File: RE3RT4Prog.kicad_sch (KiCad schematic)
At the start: 47 parts, among them J1 Conn_01x08, J2 Conn_01x08, Q1 BD140, Q2 2N7000, Q3 2N7000, Q4 2N7000, U1 DG408, U2 155RE3, U3 556RT4, U4 74HC164

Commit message: Schema almost done
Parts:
- added C1, C2: 22, symbol Device:C
- added C3: 0.1, symbol Device:C
- added C4, C5, C7, C8, C9: 1.0, symbol Device:C
- added C6: 10.0, symbol Device:C
- added J3: DE9_Receptacle_MountingHoles, Connector_Dsub:DSUB-9_Female_Horizontal_P2.77x2.84mm_EdgePinOffset4.94mm_Housed_MountingHolesOffset7.48mm, symbol Connector:DE9_Receptacle_MountingHoles
- added J4, J5: Conn_01x02, Connector_PinHeader_2.54mm:PinHeader_1x02_P2.54mm_Vertical, symbol Connector_Generic:Conn_01x02
- added J6: PicKit, Connector_PinHeader_2.54mm:PinHeader_1x05_P2.54mm_Vertical, symbol Connector_Generic:Conn_01x05
- added J7: Barrel_Jack_MountingPin, Connector_BarrelJack:BarrelJack_GCT_DCJ200-10-A_Horizontal, symbol Connector:Barrel_Jack_MountingPin
- added TP12: +5V, symbol Connector:TestPoint
- added TP13: GND, symbol Connector:TestPoint
- added TP14: +12V, symbol Connector:TestPoint
- added U6: PIC18F26K22-xSP, Package_DIP:DIP-28_W7.62mm_Socket_LongPads, symbol MCU_Microchip_PIC18:PIC18F26K22-xSP
- added U7: MAX232, Package_DIP:DIP-16_W7.62mm_Socket_LongPads, symbol Interface_UART:MAX232
- added Y1: 7.3728, Crystal:Crystal_HC49-U_Vertical, symbol Device:Crystal
- R15: value R -> 2k
- R16: value R -> 100k
- R17, R18: value R -> 100
- R19, R20: value R -> 22
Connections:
- net +12V: now also TP14.1
- net +5V: now also C7.1, J4.1 (Pin_1), J4.2 (Pin_2), J6.2 (Pin_2), J7.1, TP12.1, U7.16 (VCC)
- net B0: now also U6.21 (RB0)
- net B1: now also U6.22 (RB1)
- net B2: now also U6.23 (RB2)
- net CE: now also U6.13 (RC2)
- net CLK: now also U6.14 (RC3)
- net CLR: now also U6.15 (RC4)
- net GND: now also R17.2, R18.2, C1.2, C2.2, C3.2, C6.2, C7.2, C8.2, C9.2, J3.0 (PAD), J3.5, J5.1 (Pin_1), J5.2 (Pin_2), J6.3 (Pin_3), J7.2, TP13.1, U6.19 (VSS), U6.8 (VSS), U7.15 (GND)
- net RD: now also U6.25 (RB4)
- net SER: now also U6.16 (RC5)
- net WR: now also U6.24 (RB3)
- net at R17.1: now also U7.10 (T2IN)
- net at R19.1: now also U7.14 (T1OUT)
- net at R19.2: now also J3.2
- net at R18.1: now also U7.8 (R2IN)
- net at R16.1: now also C3.1, U6.20 (VDD)
- net at R16.2: now also R15.2, C6.1
- net MCLR: now reaches R15.1
- net MCLR: now also J6.1 (Pin_1), U6.1 (~{MCLR}/VPP/RE3)
- net at R20.1: now also U7.13 (R1IN)
- net at R20.2: now also J3.3
- new net: C2.1, U6.10 (RA6/OSC2_CLKOUT), Y1.1
- new net: C1.1, U6.9 (RA7/OSC1_CLKIN), Y1.2
- new net: C8.1, U7.2 (VS+)
- new net: C5.1, U7.4 (C2+)
- new net: C5.2, U7.5 (C2-)
- new net: C4.1, U7.1 (C1+)
- new net: C4.2, U7.3 (C1-)
- new net: C9.1, U7.6 (VS-)
- new net PGC: J6.5 (Pin_5), U6.27 (RB6/PGC)
- new net PGD: J6.4 (Pin_4), U6.28 (RB7/PGD)
- new net RX: U6.18 (RC7), U7.12 (R1OUT)
- new net TX: U6.17 (RC6), U7.11 (T1IN)
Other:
- moved on the sheet: R15, R16, R17, R18, R19, R20

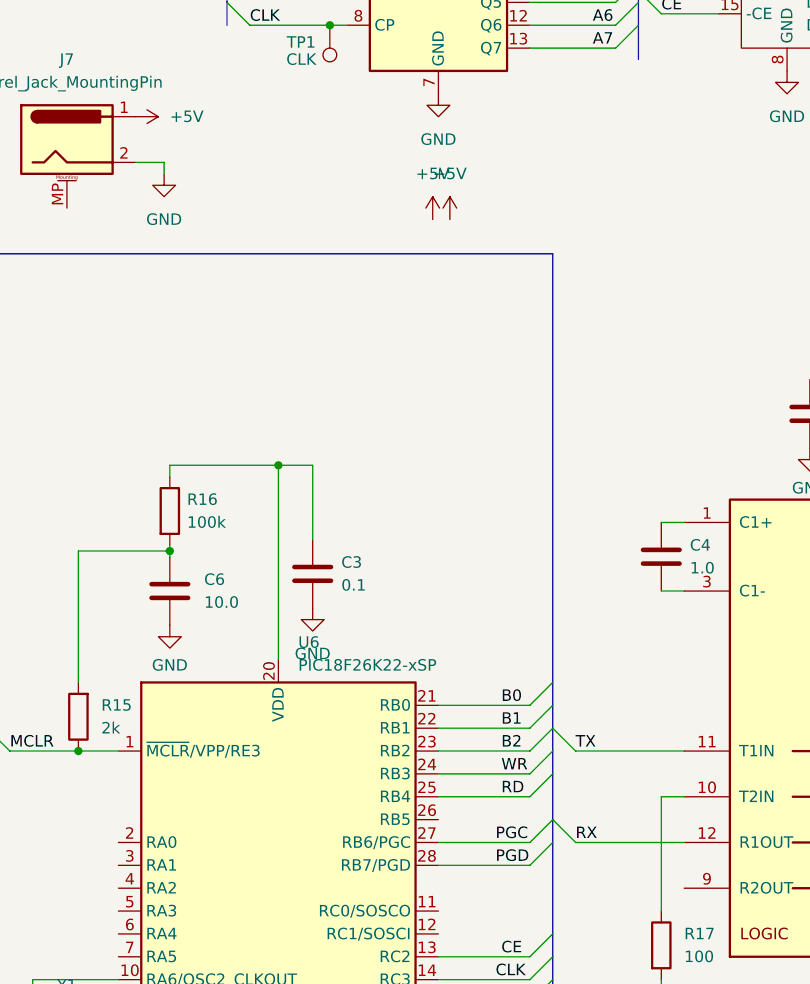
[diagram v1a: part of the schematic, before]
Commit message: Schema done with fottprints
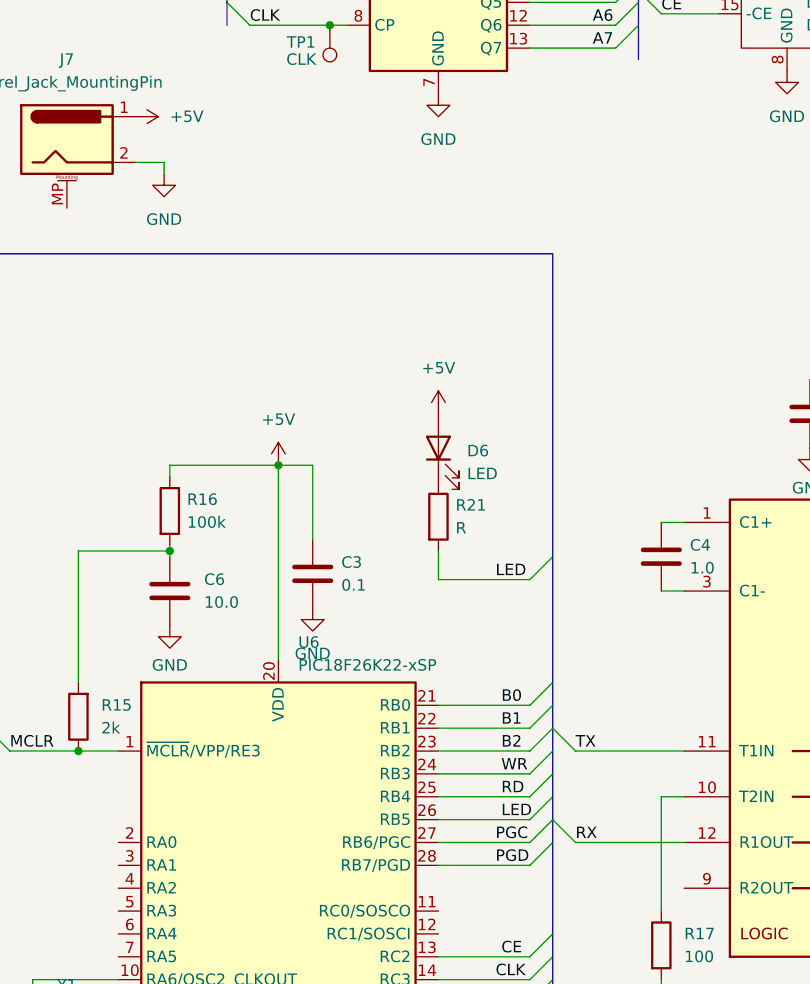
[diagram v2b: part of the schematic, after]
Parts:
- added D6: LED, LED_THT:LED_D5.0mm, symbol Device:LED
- added R21: R, Resistor_THT:R_Axial_DIN0207_L6.3mm_D2.5mm_P10.16mm_Horizontal, symbol Device:R
- C1, C2, C3, C4, C5, C6, C7, C8, C9: footprint (none) -> Capacitor_THT:C_Disc_D4.3mm_W1.9mm_P5.00mm
- D3, D4, D5: footprint (none) -> LED_THT:LED_D5.0mm
- J1, J2: footprint (none) -> Connector_PinHeader_2.54mm:PinHeader_1x08_P2.54mm_Vertical
- R1, R10, R11, R12, R13, R14, R15, R16, R17, R18, R19, R2, R20, R3, R4, R5, R6, R7, R8, R9: footprint (none) -> Resistor_THT:R_Axial_DIN0207_L6.3mm_D2.5mm_P10.16mm_Horizontal
- TP1, TP10, TP11, TP12, TP13, TP14, TP2, TP3, TP4, TP5, TP6, TP7, TP8, TP9: footprint (none) -> TestPoint:TestPoint_Loop_D3.50mm_Drill0.9mm_Beaded
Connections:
- net +5V: now also C3.1, R16.1, U6.20 (VDD), D6.2 (A)
- net LED: now reaches U6.26 (RB5)
- net LED: now also R21.2
- new net: D6.1 (K), R21.1

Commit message: Work in progress
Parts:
- C1, C2: footprint Capacitor_THT:C_Disc_D4.3mm_W1.9mm_P5.00mm -> Capacitor_THT:C_Disc_D3.4mm_W2.1mm_P2.50mm
- C3: footprint Capacitor_THT:C_Disc_D4.3mm_W1.9mm_P5.00mm -> Capacitor_SMD:C_0603_1608Metric_Pad1.08x0.95mm_HandSolder
- J4: value Conn_01x02 -> +5V
- J5: value Conn_01x02 -> GND
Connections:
- net B0: now also TP6.1
- net B1: now also TP7.1
- net B2: now also TP8.1
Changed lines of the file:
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@@
+    (effects (font (size 1.27 1.27)) (justify left bottom))
+  )
+  (label "B1" (at 274.955 144.78 0) (fields_autoplaced)
     (effects (font (size 1.27 1.27)) (justify left bottom))
   )
@@
     (effects (font (size 1.27 1.27)) (justify left bottom))
   )
+  (label "B0" (at 274.955 139.7 0) (fields_autoplaced)
+    (effects (font (size 1.27 1.27)) (justify left bottom))
+  )
   (label "D7" (at 274.955 83.185 0) (fields_autoplaced)
     (effects (font (size 1.27 1.27)) (justify left bottom))
@@
   )
   (label "D3" (at 170.815 43.18 0) (fields_autoplaced)
+    (effects (font (size 1.27 1.27)) (justify left bottom))
+  )
+  (label "B2" (at 274.955 149.86 0) (fields_autoplaced)
     (effects (font (size 1.27 1.27)) (justify left bottom))
   )
@@
       (effects (font (size 1.27 1.27)) (justify right))
     )
-    (property "Value" "Conn_01x02" (at 139.7 71.12 90)
+    (property "Value" "+5V" (at 139.7 71.12 90)
       (effects (font (size 1.27 1.27)) (justify right))
     )
@@
       (effects (font (size 1.27 1.27)) (justify left))
     )
-    (property "Value" "Conn_01x02" (at 167.64 88.9 0)
+    (property "Value" "GND" (at 167.64 88.9 0)
       (effects (font (size 1.27 1.27)) (justify left))
     )
@@
       (effects (font (size 1.27 1.27)) (justify left))
     )
-    (property "Footprint" "Capacitor_THT:C_Disc_D4.3mm_W1.9mm_P5.00mm" (at 39.0652 177.165 0)
+    (property "Footprint" "Capacitor_THT:C_Disc_D3.4mm_W2.1mm_P2.50mm" (at 39.0652 177.165 0)
       (effects (font (size 1.27 1.27)) hide)
     )
@@
       (effects (font (size 1.27 1.27)) (justify left))
     )
-    (property "Footprint" "Capacitor_THT:C_Disc_D4.3mm_W1.9mm_P5.00mm" (at 70.1802 118.11 0)
+    (property "Footprint" "Capacitor_SMD:C_0603_1608Metric_Pad1.08x0.95mm_HandSolder" (at 70.1802 118.11 0)
       (effects (font (size 1.27 1.27)) hide)
     )
@@
       (effects (font (size 1.27 1.27)) (justify left))
     )
-    (property "Footprint" "Capacitor_THT:C_Disc_D4.3mm_W1.9mm_P5.00mm" (at 46.6852 177.165 0)
-      (effects (font (size 1.27 1.27)) hide)
-    )
+    (property "Footprint" "Capacitor_THT:C_Disc_D3.4mm_W2.1mm_P2.50mm" (at 46.6852 177.165 0)
+      (effects (font (size 1.27 1.27)) hide)
+    )

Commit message: Work in progress
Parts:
- R1, R12, R21, R8: value R -> 1k
- R13: value R -> 100k
- R3, R7: value R -> 10k
- R4: value R -> 470
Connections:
- net +12V: now also R3.1
- net at Q1.2 (C), R14.2, TP9.1: no longer R3.1
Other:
- moved on the sheet: R3, R4

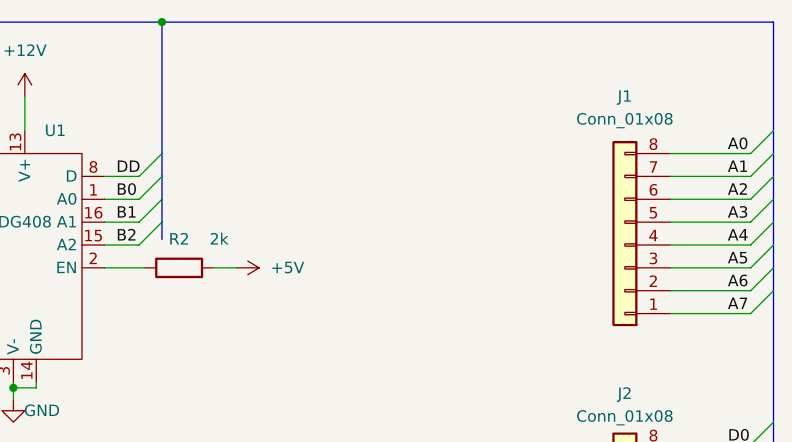
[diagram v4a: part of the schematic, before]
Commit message: Works with RT4 and RE3, but PCB needs to be updated
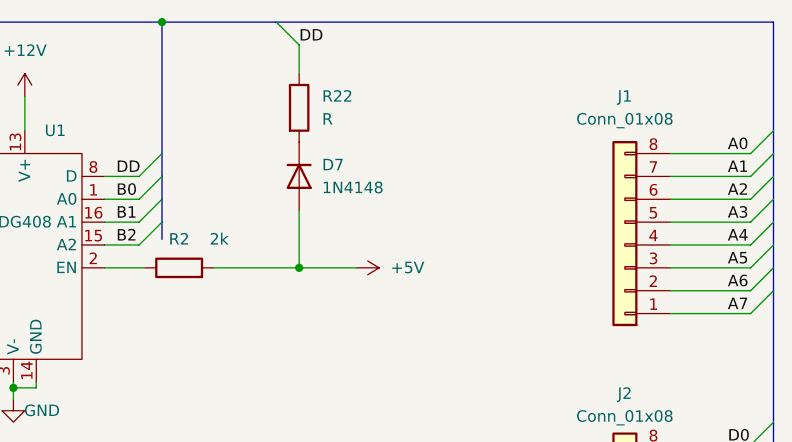
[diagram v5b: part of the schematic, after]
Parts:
- added D7: 1N4148, Diode_THT:D_DO-35_SOD27_P7.62mm_Horizontal, symbol Diode:1N4148
- added R22: R, symbol Device:R
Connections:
- net +5V: now also D7.2 (A)
- net DD: now also R22.1
- new net: D7.1 (K), R22.2
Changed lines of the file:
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@@
 	)
 	(junction
+		(at 227.33 45.72)
+		(diameter 0)
+		(color 0 0 0 0)
+	)
+	(junction
 		(at 189.23 67.31)
 		(diameter 0)
@@
 	)
 	(bus_entry
+		(at 224.79 18.415)
+		(size 2.54 2.54)
+		(stroke
+			(width 0)
+			(type default)
+		)
+	)
+	(bus_entry
 		(at 209.55 40.64)
 		(size 2.54 -2.54)
@@
 	(bus
 		(pts
+			(xy 224.79 18.415) (xy 280.035 18.415)
+		)
+		(stroke
+			(width 0)
+			(type default)
+		)
+	)
+	(bus
+		(pts
 			(xy 59.69 18.415) (xy 88.265 18.415)
 		)
@@
 	(wire
 		(pts
+			(xy 227.33 45.72) (xy 233.68 45.72)
+		)
+		(stroke
+			(width 0)
+			(type default)
+		)
+	)
+	(wire
+		(pts
 			(xy 168.91 159.385) (xy 168.91 167.64)
 		)
@@
 		)
 	)
+	(wire
+		(pts
+			(xy 227.33 39.37) (xy 227.33 45.72)
+		)
+		(stroke
+			(width 0)
+			(type default)
+		)
+	)
 	(bus
 		(pts
@@
 	(wire
 		(pts
+			(xy 227.33 20.955) (xy 227.33 24.13)
+		)
+		(stroke
+			(width 0)
+			(type default)
+		)
+	)
+	(wire
+		(pts
 			(xy 83.185 133.985) (xy 93.345 133.985)
 		)
@@
 	(wire
 		(pts
-			(xy 217.805 45.72) (xy 220.345 45.72)
+			(xy 217.805 45.72) (xy 227.33 45.72)
 		)
 		(stroke
@@
 	(bus
 		(pts
-			(xy 212.09 18.415) (xy 280.035 18.415)
+			(xy 212.09 18.415) (xy 224.79 18.415)
 		)
 		(stroke
@@
 		)
 	)
+	(label "DD"
+		(at 227.33 20.955 0)
+		(fields_autoplaced yes)
+		(effects
+			(font
+				(size 1.27 1.27)
+			)
+			(justify left bottom)
+		)
+	)
 	(label "A2"
 		(at 107.95 43.18 0)
@@
 	)
 	(symbol
+		(lib_id "Diode:1N4148")
+		(at 227.33 35.56 270)
+		(unit 1)
+		(exclude_from_sim no)
+		(in_bom yes)
+		(on_board yes)
+		(dnp no)
+		(fields_autoplaced yes)
+		(property "Reference" "D7"
+			(at 229.87 34.2899 90)
+			(effects
+				(font
+					(size 1.27 1.27)
+				)
+				(justify left)
+			)
+		)
+		(property "Value" "1N4148"
+			(at 229.87 36.8299 90)
+			(effects
+				(font
+					(size 1.27 1.27)
+				)
+				(justify left)
+			)
+		)
+		(property "Footprint" "Diode_THT:D_DO-35_SOD27_P7.62mm_Horizontal"
+			(at 227.33 35.56 0)
+			(effects
+				(font
+					(size 1.27 1.27)
+				)
+				(hide yes)
+			)
+		)
+		(property "Datasheet" "https://assets.nexperia.com/documents/data-sheet/1N4148_1N4448.pdf"
+			(at 227.33 35.56 0)
+			(effects
+				(font
+					(size 1.27 1.27)
+				)
+				(hide yes)
+			)
+		)
+		(property "Description" "100V 0.15A standard switching diode, DO-35"
+			(at 227.33 35.56 0)
+			(effects
+				(font
+					(size 1.27 1.27)
+				)
+				(hide yes)
+			)
+		)
+		(property "Sim.Device" "D"
+			(at 227.33 35.56 0)
+			(effects
+				(font
+					(size 1.27 1.27)
+				)
+				(hide yes)
+			)
+		)
+		(property "Sim.Pins" "1=K 2=A"
+			(at 227.33 35.56 0)
+			(effects
+				(font
+					(size 1.27 1.27)
+				)
+				(hide yes)
+			)
+		)
+		(pin "1"
+		)
+		(pin "2"
+		)
+		(instances
+			(project ""
+				(path "/d162d97a-69b3-496a-a822-43acfab3a7ae"
+					(reference "D7")
+					(unit 1)
+				)
+			)
+		)
+	)
+	(symbol
 		(lib_id "power:+5V")
 		(at 230.505 89.535 0)
@@
 	(symbol
 		(lib_id "power:+5V")
-		(at 220.345 45.72 270)
+		(at 233.68 45.72 270)
 		(unit 1)
 		(exclude_from_sim no)
@@
 		(fields_autoplaced yes)
 		(property "Reference" "#PWR017"
-			(at 216.535 45.72 0)
+			(at 229.87 45.72 0)
 			(effects
 				(font
@@
 		)
 		(property "Value" "+5V"
-			(at 224.155 45.72 90)
+			(at 237.49 45.72 90)
 			(effects
 				(font
@@
 		)
 		(property "Footprint" ""
-			(at 220.345 45.72 0)
+			(at 233.68 45.72 0)
 			(effects
 				(font
@@
 		)
 		(property "Datasheet" ""
-			(at 220.345 45.72 0)
+			(at 233.68 45.72 0)
 			(effects
 				(font
@@
 		)
 		(property "Description" ""
-			(at 220.345 45.72 0)
+			(at 233.68 45.72 0)
 			(effects
 				(font
@@
 					(unit 1)
 				)
+			)
+		)
+	)
+	(symbol
+		(lib_id "Device:R")
+		(at 227.33 27.94 0)
+		(unit 1)
+		(exclude_from_sim no)
+		(in_bom yes)
+		(on_board yes)
+		(dnp no)
+		(fields_autoplaced yes)
+		(property "Reference" "R22"
+			(at 229.87 26.6699 0)
+			(effects
+				(font
+					(size 1.27 1.27)
+				)
+				(justify left)
+			)
+		)
+		(property "Value" "R"
+			(at 229.87 29.2099 0)
+			(effects
+				(font
+					(size 1.27 1.27)
+				)
+				(justify left)
+			)
+		)
+		(property "Footprint" ""
+			(at 225.552 27.94 90)
+			(effects
+				(font
+					(size 1.27 1.27)
+				)
+				(hide yes)
+			)
+		)
+		(property "Datasheet" "~"
+			(at 227.33 27.94 0)
+			(effects
+				(font
+					(size 1.27 1.27)
+				)
+				(hide yes)
+			)
+		)
+		(property "Description" "Resistor"
+			(at 227.33 27.94 0)
+			(effects
+				(font
+					(size 1.27 1.27)
+				)
+				(hide yes)
+			)
+		)
+		(pin "2"
+		)
+		(pin "1"
+		)
+		(instances
+			(project ""
+				(path "/d162d97a-69b3-496a-a822-43acfab3a7ae"
+					(reference "R22")
+					(unit 1)
+				)
